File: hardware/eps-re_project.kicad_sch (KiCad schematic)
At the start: 18 parts, among them J1 53398-0471, J10 53398-0471, J11 53398-0471, J12 53398-0671, J13 53398-0671, J14 53398-0471, J2 53398-0471, J3 53398-0671, J4 53398-0471, J5 53398-0471, J6 53398-0471, J7 53398-0471, J8 53398-0671, J9 53398-0471

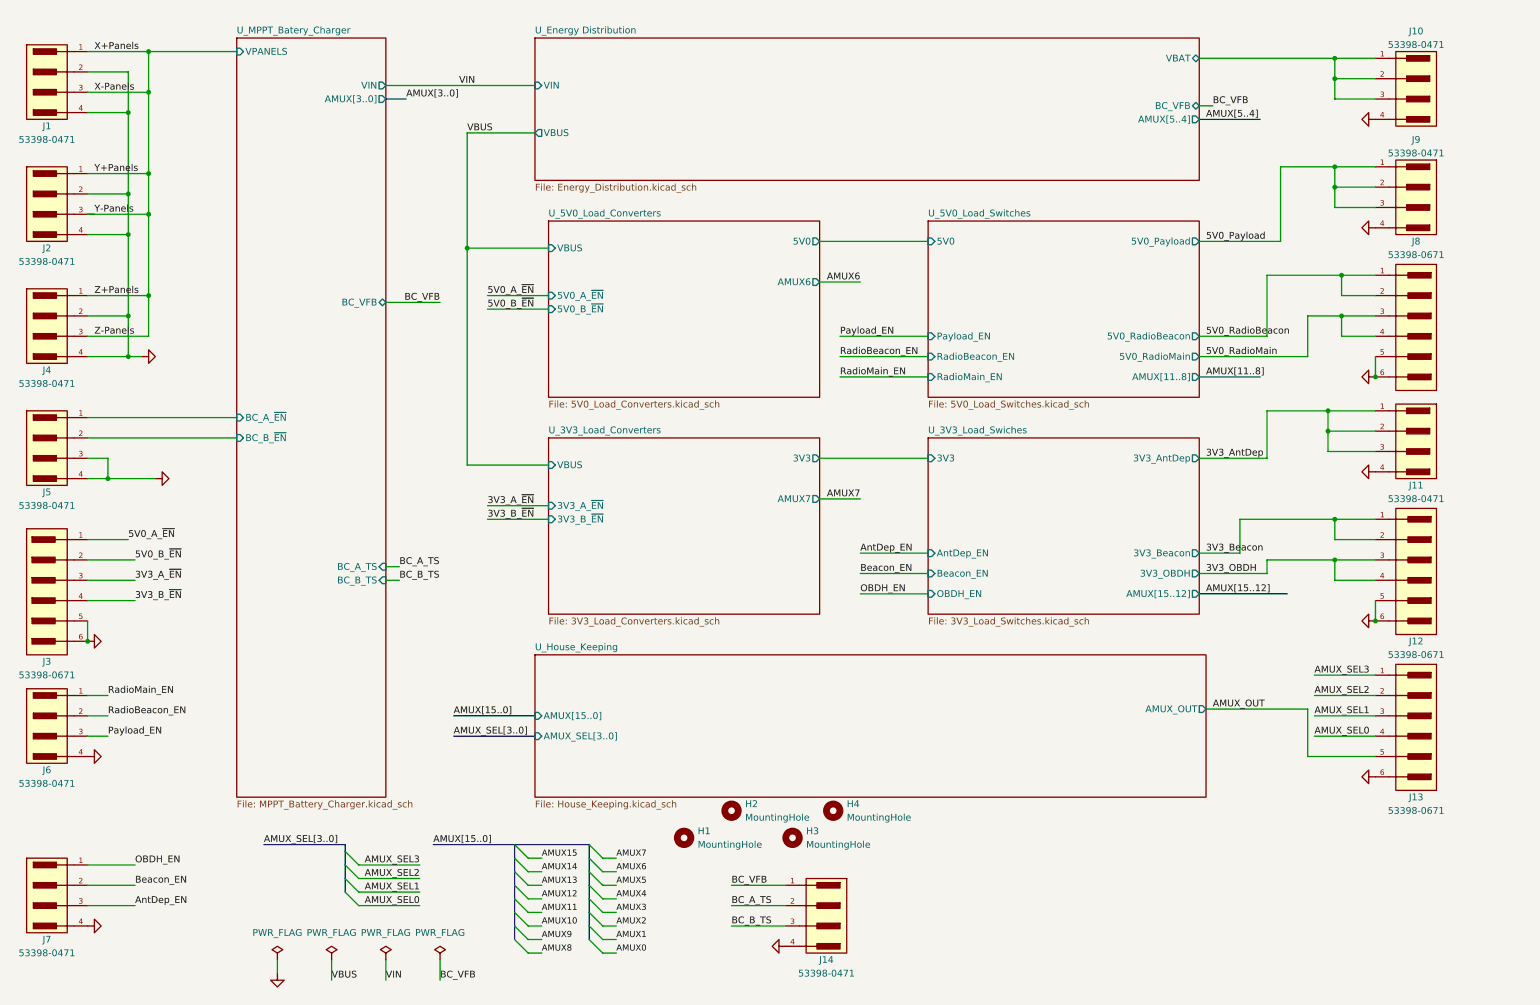
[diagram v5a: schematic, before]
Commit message: hardware: Updating the schematic and layout to solve #8, #9 and #10.
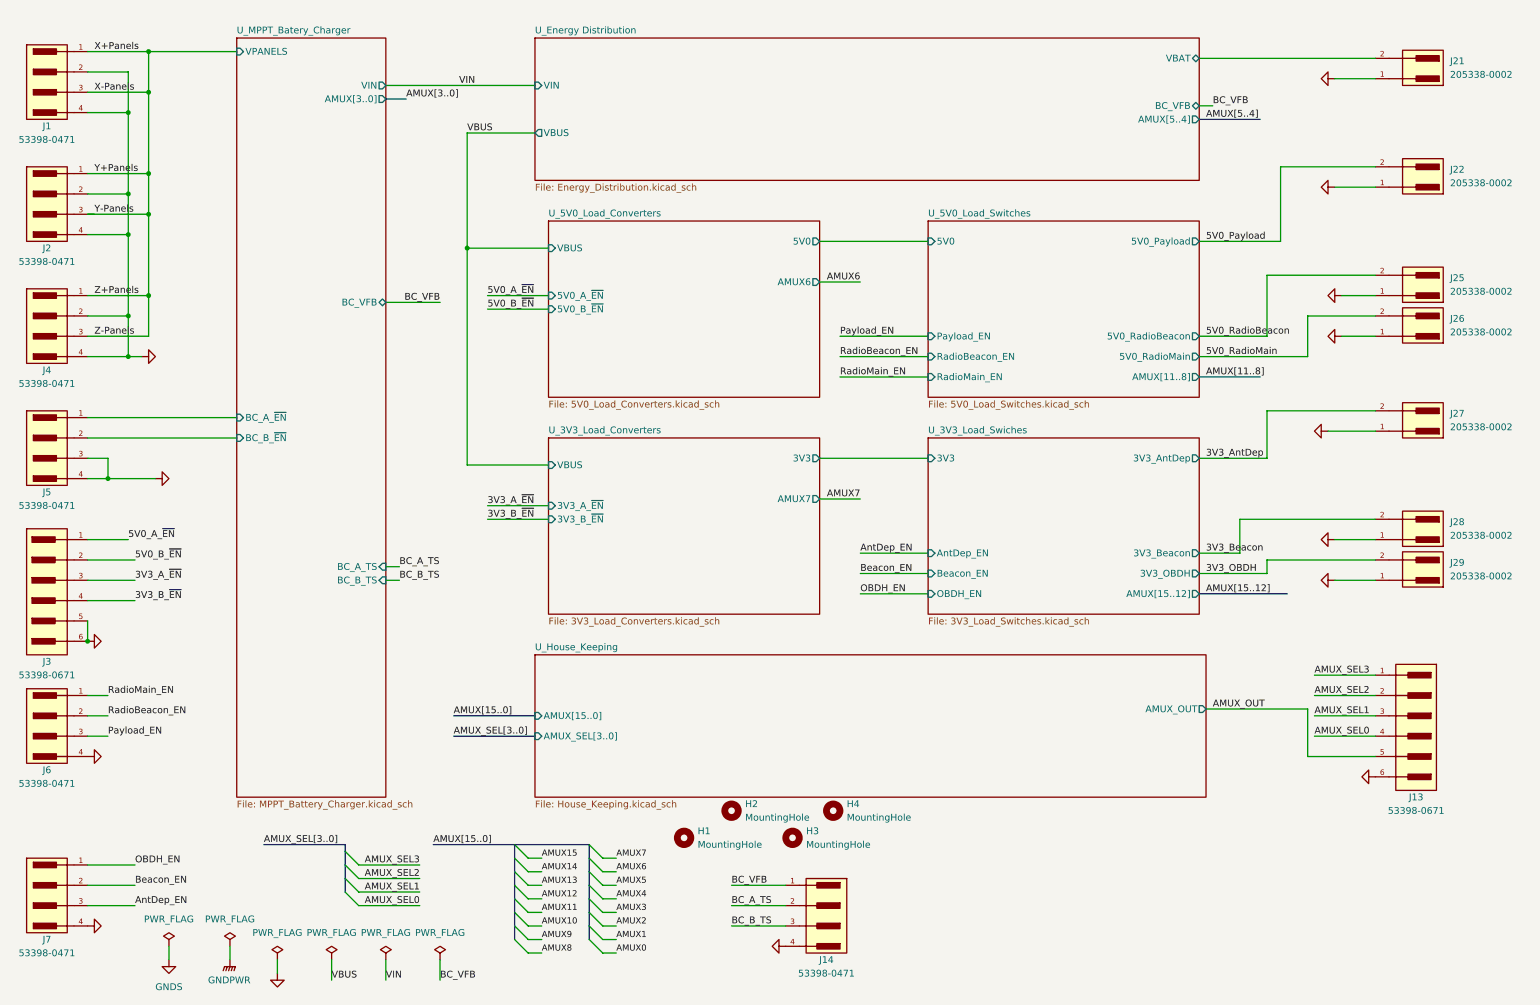
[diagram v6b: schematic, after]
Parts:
- removed J10, J11, J9: 53398-0471, footprints:533980471, symbol 533980471:533980471_1
- removed J12, J8: 53398-0671, footprints:533980671, symbol 533980671:53398-0671
- added J21, J22, J25, J26, J27, J28, J29: 205338-0002, footprints:2053380002, symbol 2053380002:2053380002
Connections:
- net 3V3_AntDep: now also J27.2
- net 3V3_Beacon: now also J28.2
- net 3V3_OBDH: now also J29.2
- net 5V0_Payload: now also J22.2
- net 5V0_RadioBeacon: now also J25.2
- net 5V0_RadioMain: now also J26.2
- net GND: now also J21.1, J22.1, J25.1, J26.1, J27.1, J28.1, J29.1
- net U_Energy Distribution/VBAT: now also J21.2

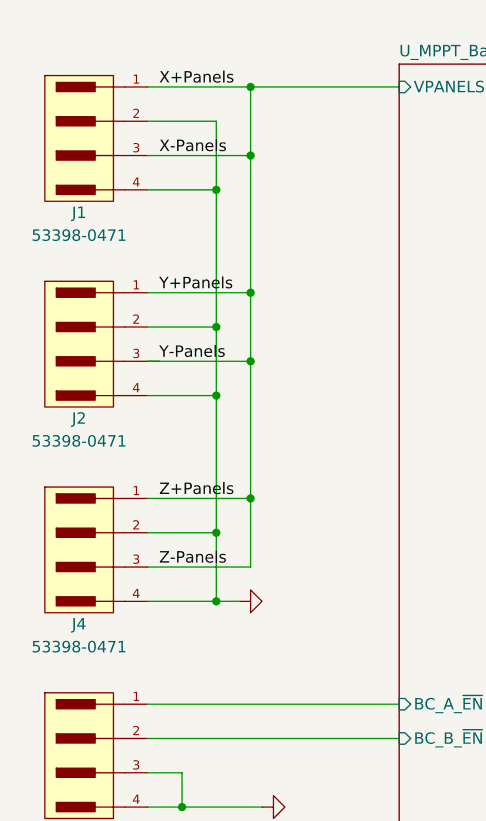
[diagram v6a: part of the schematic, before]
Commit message: hardware: Making corrections regarding #15, #14, #13 and starting #12 and #11.
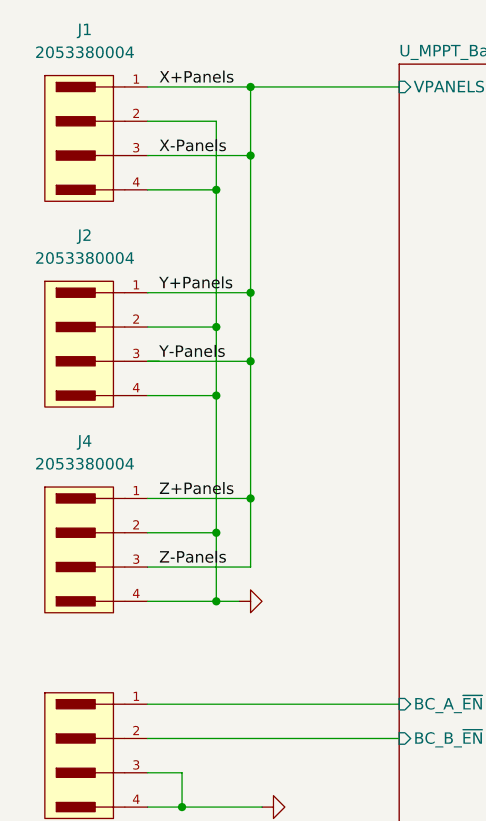
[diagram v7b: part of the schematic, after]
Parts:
- removed J1, J2, J4: 53398-0471, footprints:533980471, symbol 533980471:533980471_1
- added J1, J2, J4: 2053380004, footprints:2053380004, symbol 2053380004:2053380004
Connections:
- net GND: now also J1.2, J1.4, J2.2, J2.4, J4.2, J4.4
- net X+Panels: now also J1.1, J1.3, J2.1, J2.3, J4.1, J4.3

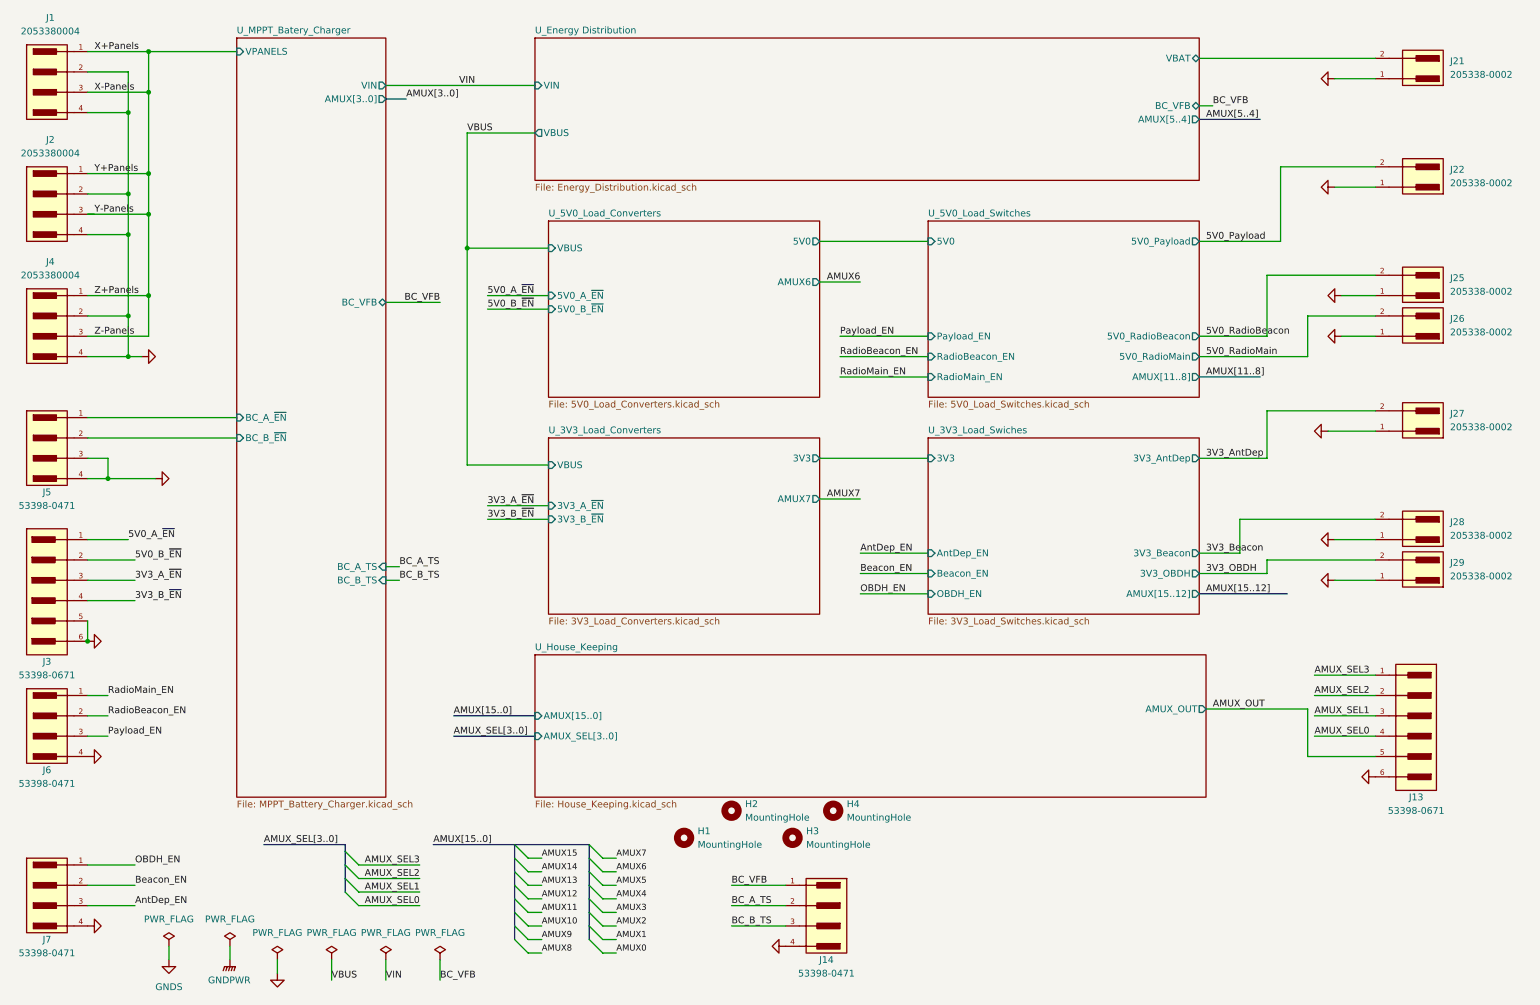
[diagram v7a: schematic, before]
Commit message: hardware: Updating the MPPT circuit.
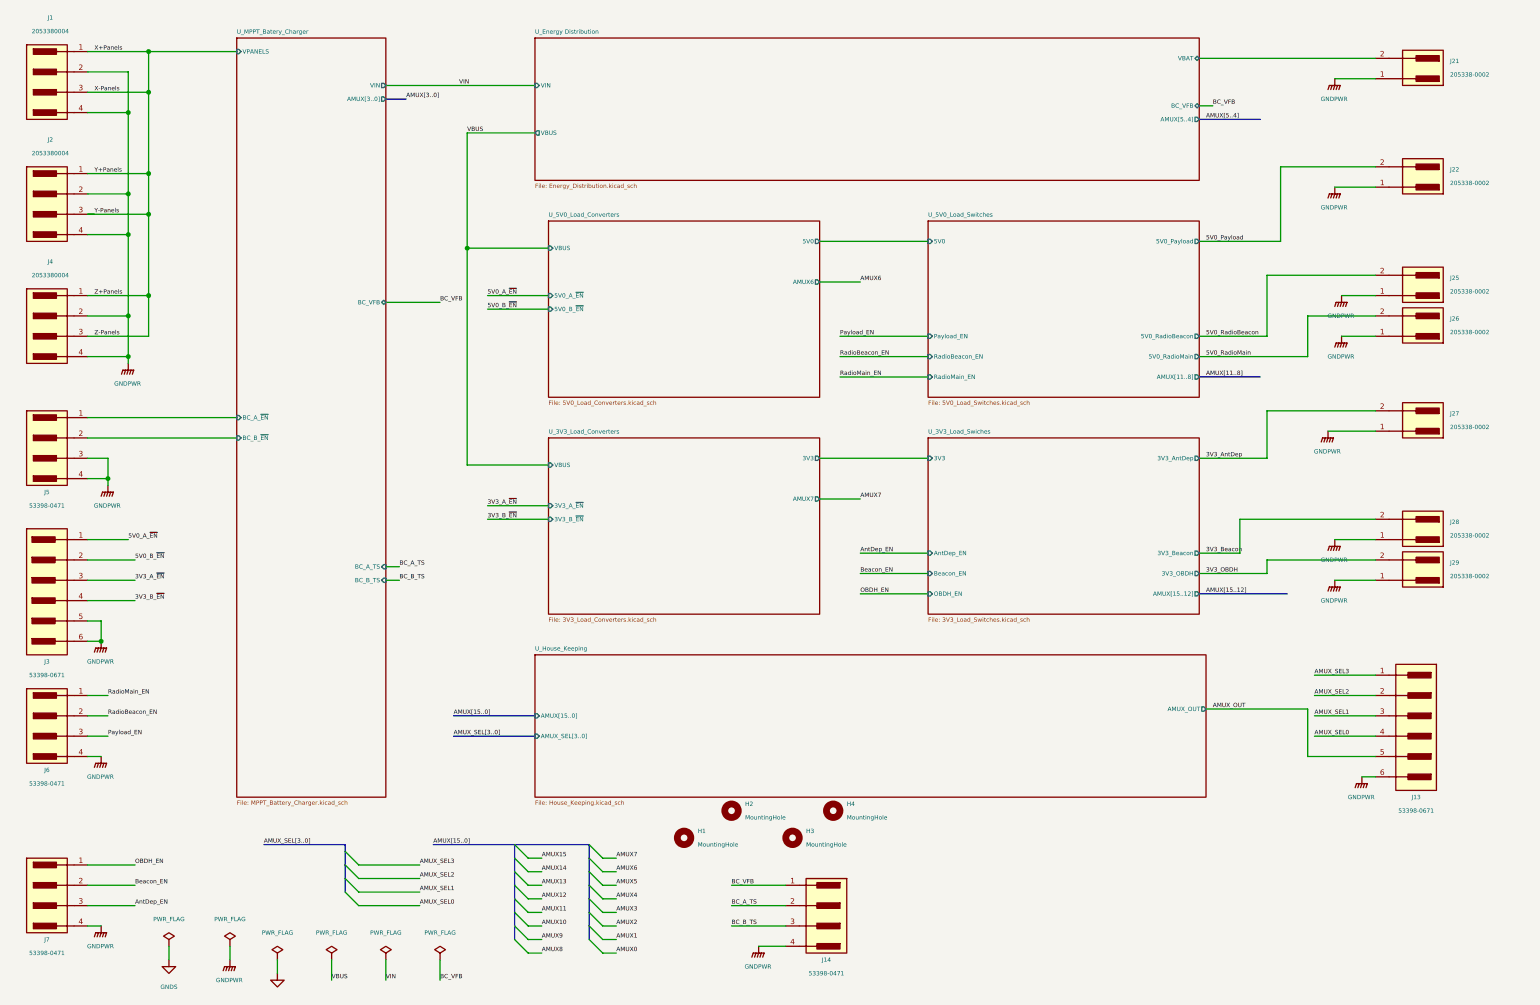
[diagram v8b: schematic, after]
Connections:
- net GND: no longer J1.2, J1.4, J13.6, J14.4, J2.2, J2.4, J21.1, J22.1, J25.1, J26.1, J27.1, J28.1, J29.1, J3.5, J3.6, J4.2, J4.4, J5.3, J5.4, J6.4, J7.4
- net GNDPWR: now also J1.2, J1.4, J13.6, J14.4, J2.2, J2.4, J21.1, J22.1, J25.1, J26.1, J27.1, J28.1, J29.1, J3.5, J3.6, J4.2, J4.4, J5.3, J5.4, J6.4, J7.4
